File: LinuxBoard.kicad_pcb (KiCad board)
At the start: 2 copper layers, 5 parts, among them J1 Wuerth_7499010121A, U1 STM32MP151AAB3, U2 MT41K64M16TW-107_AAT_J_TR, U3 DP83848C, U4 STPMIC1APQR

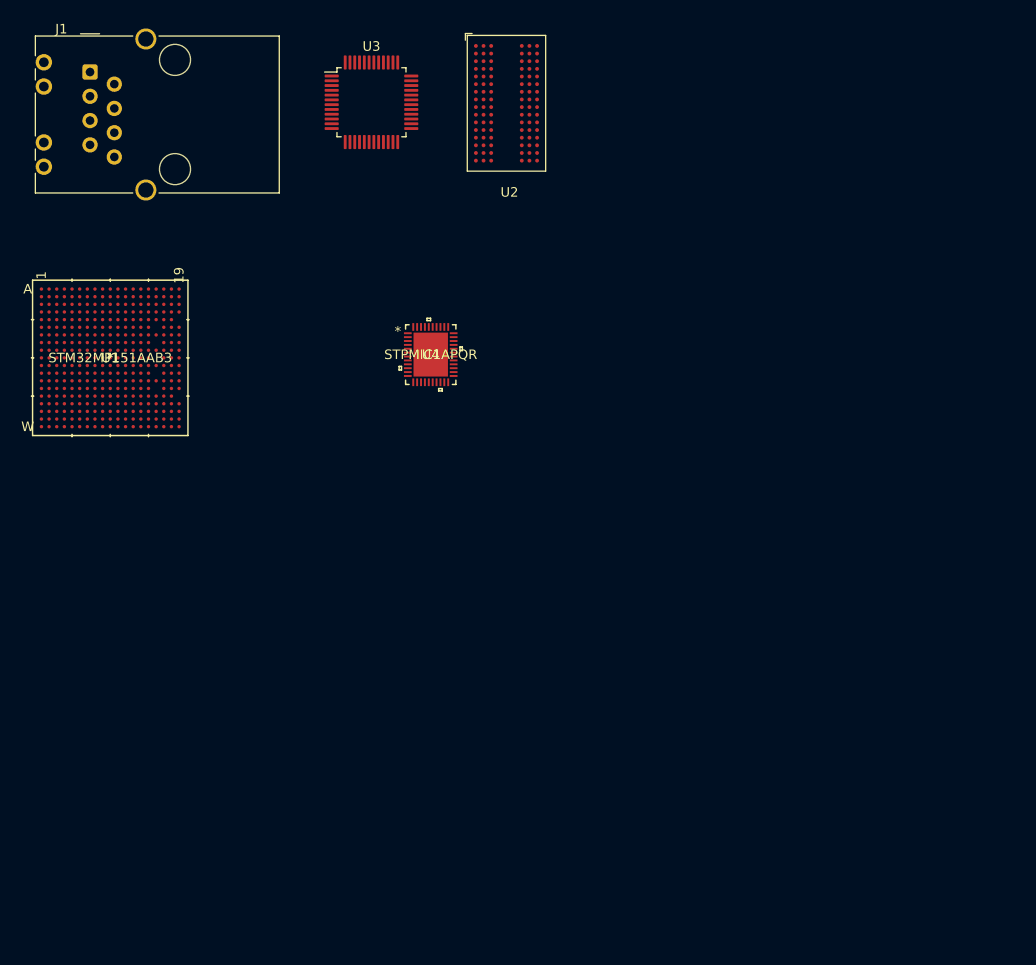
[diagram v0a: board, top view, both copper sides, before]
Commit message: Add bulk labels for RAM and ethernet
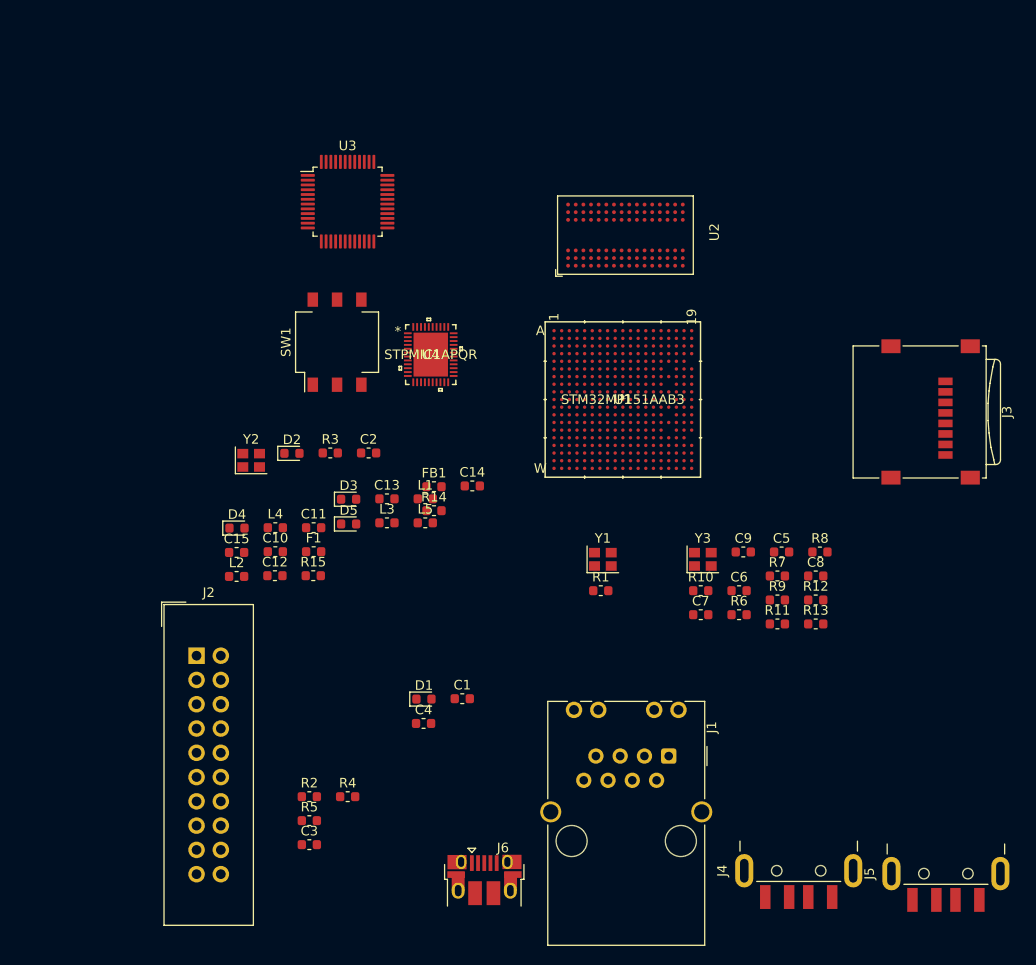
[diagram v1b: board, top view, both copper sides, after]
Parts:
- added C1: C, Capacitor_SMD:C_0603_1608Metric, F.Cu at (123.9, 100.9)
- added C10: C, Capacitor_SMD:C_0603_1608Metric, F.Cu at (104.3, 85.5)
- added C11: C, Capacitor_SMD:C_0603_1608Metric, F.Cu at (108.3, 83.0)
- added C12: C, Capacitor_SMD:C_0603_1608Metric, F.Cu at (104.3, 88.0)
- added C13: C, Capacitor_SMD:C_0603_1608Metric, F.Cu at (116.0, 80.0)
- added C14: C, Capacitor_SMD:C_0603_1608Metric, F.Cu at (125.0, 78.6)
- added C15: C, Capacitor_SMD:C_0603_1608Metric, F.Cu at (100.3, 85.6)
- added C2: C, Capacitor_SMD:C_0603_1608Metric, F.Cu at (114.1, 75.2)
- added C3: C, Capacitor_SMD:C_0603_1608Metric, F.Cu at (107.9, 116.2)
- added C4: C, Capacitor_SMD:C_0603_1608Metric, F.Cu at (119.8, 103.5)
- added C5: C, Capacitor_SMD:C_0603_1608Metric, F.Cu at (157.3, 85.5)
- added C6: C, Capacitor_SMD:C_0603_1608Metric, F.Cu at (152.9, 89.6)
- added C7: C, Capacitor_SMD:C_0603_1608Metric, F.Cu at (148.8, 92.1)
- added C8: C, Capacitor_SMD:C_0603_1608Metric, F.Cu at (160.9, 88.1)
- added C9: C, Capacitor_SMD:C_0603_1608Metric, F.Cu at (153.3, 85.5)
- added D1: LED, LED_SMD:LED_0603_1608Metric, F.Cu at (119.9, 100.9)
- added D2: LED, LED_SMD:LED_0603_1608Metric, F.Cu at (106.1, 75.2)
- added D3: D_Schottky, Diode_SMD:D_0603_1608Metric, F.Cu at (112.0, 80.0)
- added D4: LED, LED_SMD:LED_0603_1608Metric, F.Cu at (100.3, 83.0)
- added D5: LED, LED_SMD:LED_0603_1608Metric, F.Cu at (112.0, 82.6)
- added F1: Fuse, Fuse:Fuse_0603_1608Metric, F.Cu at (108.3, 85.5)
- added FB1: Ferrite_Bead, Inductor_SMD:L_0603_1608Metric, F.Cu at (120.9, 78.7)
- added J2: Conn_02x10_Counter_Clockwise, Connector_IDC:IDC-Header_2x10_P2.54mm_Vertical, F.Cu at (96.1, 96.4)
- added J3: Micro_SD_Card, Connector_Card:microSD_HC_Wuerth_693072010801, F.Cu at (172.9, 70.9)
- added J4: USB_A, Connector_USB:USB_A_CNCTech_1001-011-01101_Horizontal, F.Cu at (159.1, 112.0)
- added J5: USB_A, Connector_USB:USB_A_CNCTech_1001-011-01101_Horizontal, F.Cu at (174.5, 112.3)
- added J6: USB_B_Micro, Connector_USB:USB_Micro-B_Amphenol_10103594-0001LF_Horizontal, F.Cu at (126.2, 119.9)
- added L1: L, Inductor_SMD:L_0603_1608Metric, F.Cu at (120.0, 80.0)
- added L2: L, Inductor_SMD:L_0603_1608Metric, F.Cu at (100.3, 88.1)
- added L3: L, Inductor_SMD:L_0603_1608Metric, F.Cu at (116.0, 82.5)
- added L4: L, Inductor_SMD:L_0603_1608Metric, F.Cu at (104.3, 83.0)
- added L5: L, Inductor_SMD:L_0603_1608Metric, F.Cu at (120.0, 82.5)
- added R1: R, Resistor_SMD:R_0603_1608Metric, F.Cu at (138.4, 89.6)
- added R10: R, Resistor_SMD:R_0603_1608Metric, F.Cu at (148.8, 89.6)
- added R11: R, Resistor_SMD:R_0603_1608Metric, F.Cu at (156.9, 93.1)
- added R12: 2.2K, Resistor_SMD:R_0603_1608Metric, F.Cu at (160.9, 90.6)
- added R13: 2.2K, Resistor_SMD:R_0603_1608Metric, F.Cu at (160.9, 93.1)
- added R14: R, Resistor_SMD:R_0603_1608Metric, F.Cu at (120.9, 81.2)
- added R15: R, Resistor_SMD:R_0603_1608Metric, F.Cu at (108.3, 88.0)
- added R2: R, Resistor_SMD:R_0603_1608Metric, F.Cu at (107.9, 111.2)
- added R3: R, Resistor_SMD:R_0603_1608Metric, F.Cu at (110.1, 75.2)
- added R4: R, Resistor_SMD:R_0603_1608Metric, F.Cu at (111.9, 111.2)
- added R5: R, Resistor_SMD:R_0603_1608Metric, F.Cu at (107.9, 113.7)
- added R6: R, Resistor_SMD:R_0603_1608Metric, F.Cu at (152.9, 92.1)
- added R7: R, Resistor_SMD:R_0603_1608Metric, F.Cu at (156.9, 88.1)
- added R8: R, Resistor_SMD:R_0603_1608Metric, F.Cu at (161.3, 85.5)
- added R9: 4.87K, Resistor_SMD:R_0603_1608Metric, F.Cu at (156.9, 90.6)
- added SW1: SW_DIP_x03, Button_Switch_SMD:SW_DIP_SPSTx03_Slide_Omron_A6S-310x_W8.9mm_P2.54mm, F.Cu at (110.8, 63.6)
- added Y1: Crystal_GND24, Crystal:Crystal_SMD_2520-4Pin_2.5x2.0mm, F.Cu at (138.6, 86.3)
- added Y2: Crystal_GND24, Crystal:Crystal_SMD_2520-4Pin_2.5x2.0mm, F.Cu at (101.8, 76.0)
- added Y3: 25MHz, Crystal:Crystal_SMD_2520-4Pin_2.5x2.0mm, F.Cu at (149.1, 86.3)
- moved J1 93.7 mm to (145.5, 106.9), turned to 270 degrees
- moved U1 53.8 mm to (140.7, 69.6)
- moved U2 21.8 mm to (133.5, 52.4), turned to 90 degrees
- moved U3 10.7 mm to (111.9, 48.9)
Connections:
- net Net-(J1-Pad4) renamed /Ethernet/RD_P
- net Net-(J1-Pad6) renamed /Ethernet/RD_N
- net Net-(U1-PadA8) renamed /MPU/USART1_RX_TO_MPU
- net Net-(U1-PadB5) renamed /MPU/I2C_SDA
- net Net-(U1-PadC8) renamed /MPU/USART1_TX_FROM_MPU
- net Net-(U1-PadD7) renamed /MPU/USART2_TX_FROM_M4
- net Net-(U1-PadE3) renamed /MPU/USART2_RX_TO_M4
- net Net-(U1-PadF1) renamed /MPU/ETH1_PHY_INTN
- net Net-(U1-PadM4) renamed /RAM/A15
- net Net-(U1-PadP3) renamed /MPU/ETH1_COL
- net Net-(U1-PadP4) renamed /MPU/DAC1_OUT2
- net Net-(U1-PadR3) renamed /MPU/ETH1_CRS
- net Net-(U1-PadR4) renamed /MPU/DAC1_OUT1
- net Net-(U1-PadR7) renamed /RAM/A13
- net Net-(U1-PadT1) renamed /MPU/ETH1_TXD3
- net Net-(U1-PadT12) renamed /MPU/I2C_SCL
- net Net-(U1-PadT2) renamed /MPU/ETH1_TXD2
- net Net-(U1-PadT3) renamed /MPU/ETH1_TX_CLK
- net Net-(U1-PadT6) renamed /MPU/ETH1_RX_DV
- net Net-(U1-PadT9) renamed /MPU/ETH1_TXD1
- net Net-(U1-PadU2) renamed /MPU/ETH1_TXD0
- net Net-(U1-PadU4) renamed /MPU/ETH1_RX_CLK
- net Net-(U1-PadV1) renamed /MPU/ETH1_TX_EN
- net Net-(U1-PadV13) renamed /MPU/USB2_N
- net Net-(U1-PadV14) renamed /MPU/USB1_P
- net Net-(U1-PadV2) renamed /MPU/ETH1_MDC
- net Net-(U1-PadV3) renamed /MPU/ETH1_RXD3
- net Net-(U1-PadV4) renamed /MPU/ETH1_RXD1
- net Net-(U1-PadW13) renamed /MPU/USB2_P
- net Net-(U1-PadW14) renamed /MPU/USB1_N
- net Net-(U1-PadW2) renamed /MPU/ETH1_MDIO
- net Net-(U1-PadW3) renamed /MPU/ETH1_RXD2
- net Net-(U1-PadW4) renamed /MPU/ETH1_RXD0
- net Net-(U1-PadW5) renamed /MPU/ETH1_RX_ER
- net Net-(U2-PadA2) renamed /RAM/DQ13
- net Net-(U2-PadA3) renamed /RAM/DQ15
- net Net-(U2-PadA7) renamed /RAM/DQ12
- net Net-(U2-PadB8) renamed /RAM/DQ14
- net Net-(U2-PadC2) renamed /RAM/DQ11
- net Net-(U2-PadC3) renamed /RAM/DQ9
- net Net-(U2-PadC8) renamed /RAM/DQ10
- net Net-(U2-PadD7) renamed /RAM/DQ8
- net Net-(U2-PadE3) renamed /RAM/DQ0
- net Net-(U2-PadF2) renamed /RAM/DQ2
- net Net-(U2-PadF7) renamed /RAM/DQ1
- net Net-(U2-PadF8) renamed /RAM/DQ3
- net Net-(U2-PadG2) renamed /RAM/DQ6
- net Net-(U2-PadH3) renamed /RAM/DQ4
- net Net-(U2-PadH7) renamed /RAM/DQ7
- net Net-(U2-PadH8) renamed /RAM/DQ5
- net Net-(U3-Pad1) renamed /Ethernet/TX_CLK
- net Net-(U3-Pad2) renamed /Ethernet/TX_EN
- net Net-(U3-Pad29) renamed /Ethernet/ETH_RESET_N
- net Net-(U3-Pad3) renamed /Ethernet/TXD_0
- net Net-(U3-Pad30) renamed /Ethernet/MDIO
- net Net-(U3-Pad31) renamed /Ethernet/MDC
- net Net-(U3-Pad38) renamed /Ethernet/RX_CLK
- net Net-(U3-Pad39) renamed /Ethernet/RX_DV
- net Net-(U3-Pad4) renamed /Ethernet/TXD_1
- net Net-(U3-Pad41) renamed /Ethernet/RX_ER
- net Net-(U3-Pad43) renamed /Ethernet/RXD_0
- net Net-(U3-Pad44) renamed /Ethernet/RXD_1
- net Net-(U3-Pad45) renamed /Ethernet/RXD_2
- net Net-(U3-Pad46) renamed /Ethernet/RXD_3
- net Net-(U3-Pad5) renamed /Ethernet/TXD_2
- net Net-(U3-Pad6) renamed /Ethernet/TXD_3
- net Net-(U3-Pad7) renamed /Ethernet/ETH_PWR_DOWN
- net Net-(U4-Pad1) renamed /PMIC/PMIC_RESET_N
- net Net-(U4-Pad14) renamed /PMIC/VTT_DDR3
- net Net-(U4-Pad16) renamed /PMIC/VREF_DDR
- net Net-(U4-Pad17) renamed /PMIC/PMIC_PONKEY_N
- net Net-(U4-Pad18) renamed /PMIC/VOUT_LDO2
- net Net-(U4-Pad2) renamed /PMIC/PMIC_WAKEUP
- net Net-(U4-Pad20) renamed /PMIC/VOUT_LDO5
- net Net-(U4-Pad21) renamed /PMIC/VOUT_LDO6
- net Net-(U4-Pad23) renamed /PMIC/VOUT_LDO1
- net Net-(U4-Pad3) renamed /PMIC/I2C_SDA
- net Net-(U4-Pad38) renamed /PMIC/VBUS_HOST
- net Net-(U4-Pad39) renamed /PMIC/VDD_USB
- net Net-(U4-Pad4) renamed /PMIC/I2C_SCL
- net Net-(U4-Pad43) renamed /PMIC/PMIC_INT_N
- net Net-(U4-Pad44) renamed /PMIC/PMIC_PWRCTRL
- J1 pad 1: Net-(J1-Pad1) -> /Ethernet/TD_P
- J1 pad 10: Net-(J1-Pad10) -> /Ethernet/LED_GREEN
- J1 pad 12: Net-(J1-Pad12) -> /Ethernet/LED_YELLOW
- J1 pad 2: Net-(J1-Pad2) -> /Ethernet/RCT
- J1 pad 3: Net-(J1-Pad3) -> /Ethernet/TD_N
- J1 pad 5: Net-(J1-Pad5) -> /Ethernet/RCT
- J1 pad 8: Net-(J1-Pad8) -> GND
- J1 pad SH: Net-(J1-PadSH) -> GND
- U1 pad A10: Net-(U1-PadA10) -> /MPU/SD_D1
- U1 pad A11: Net-(U1-PadA11) -> /MPU/SD_D3
- U1 pad B10: Net-(U1-PadB10) -> /MPU/SD_CMD
- U1 pad B3: Net-(U1-PadB3) -> /MPU/SD_D2
- U1 pad C10: Net-(U1-PadC10) -> /MPU/SD_CK
- U1 pad C11: Net-(U1-PadC11) -> /MPU/SD_D0
- U1 pad E7: Net-(U1-PadE7) -> /RAM/BA0
- U1 pad E9: Net-(U1-PadE9) -> /RAM/BA1
- U1 pad F17: Net-(U1-PadF17) -> Net-(U1-PadE17)
- U1 pad F19: Net-(U1-PadF19) -> Net-(U1-PadE17)
- U1 pad F4: Net-(U1-PadF4) -> /RAM/BA2
- U1 pad G17: Net-(U1-PadG17) -> Net-(U1-PadE17)
- U1 pad G18: Net-(U1-PadG18) -> Net-(U1-PadE17)
- U1 pad G19: Net-(U1-PadG19) -> Net-(U1-PadE17)
- U1 pad H17: Net-(U1-PadH17) -> Net-(U1-PadE17)
- U1 pad H18: Net-(U1-PadH18) -> Net-(U1-PadE17)
- U1 pad J16: Net-(U1-PadJ16) -> Net-(U1-PadE17)
- U1 pad J19: Net-(U1-PadJ19) -> Net-(U1-PadE17)
- U1 pad K18: Net-(U1-PadK18) -> Net-(U1-PadE17)
- U1 pad K6: Net-(U1-PadK6) -> /RAM/A0
- U1 pad L16: Net-(U1-PadL16) -> Net-(U1-PadE17)
- U1 pad L17: Net-(U1-PadL17) -> Net-(U1-PadE17)
- U1 pad L5: Net-(U1-PadL5) -> /RAM/A1
- U1 pad L7: Net-(U1-PadL7) -> /RAM/A2
- U1 pad M17: Net-(U1-PadM17) -> Net-(U1-PadE17)
- U1 pad M18: Net-(U1-PadM18) -> Net-(U1-PadE17)
- U1 pad M19: Net-(U1-PadM19) -> Net-(U1-PadE17)
- U1 pad M6: Net-(U1-PadM6) -> /RAM/A3
- U1 pad M8: Net-(U1-PadM8) -> /RAM/A4
- U1 pad N16: Net-(U1-PadN16) -> Net-(U1-PadE17)
- U1 pad N17: Net-(U1-PadN17) -> Net-(U1-PadE17)
- U1 pad N18: Net-(U1-PadN18) -> Net-(U1-PadE17)
- U1 pad N5: Net-(U1-PadN5) -> /RAM/A5
- U1 pad N7: Net-(U1-PadN7) -> /RAM/A6
- U1 pad N9: Net-(U1-PadN9) -> /RAM/A7
- U1 pad P10: Net-(U1-PadP10) -> /RAM/A11
- U1 pad P17: Net-(U1-PadP17) -> Net-(U1-PadE17)
- U1 pad P6: Net-(U1-PadP6) -> /RAM/A8
- U1 pad P8: Net-(U1-PadP8) -> /RAM/A9
- U1 pad R11: Net-(U1-PadR11) -> /RAM/A12
- U1 pad R17: Net-(U1-PadR17) -> Net-(U1-PadE17)
- U1 pad R9: Net-(U1-PadR9) -> /RAM/A10
- U2 pad A1: Net-(U2-PadA1) -> /RAM/VDDQ
- U2 pad A8: Net-(U2-PadA8) -> /RAM/VDDQ
- U2 pad A9: Net-(U2-PadA9) -> GND
- U2 pad B1: Net-(U2-PadB1) -> GND
- U2 pad B2: Net-(U2-PadB2) -> /RAM/VDD
- U2 pad B3: Net-(U2-PadB3) -> GND
- U2 pad B9: Net-(U2-PadB9) -> GND
- U2 pad C1: Net-(U2-PadC1) -> /RAM/VDDQ
- U2 pad C9: Net-(U2-PadC9) -> /RAM/VDDQ
- U2 pad D1: Net-(U2-PadD1) -> GND
- U2 pad D2: Net-(U2-PadD2) -> /RAM/VDDQ
- U2 pad D8: Net-(U2-PadD8) -> GND
- U2 pad D9: Net-(U2-PadD9) -> /RAM/VDD
- U2 pad E1: Net-(U2-PadE1) -> GND
- U2 pad E2: Net-(U2-PadE2) -> GND
- U2 pad E8: Net-(U2-PadE8) -> GND
- U2 pad E9: Net-(U2-PadE9) -> /RAM/VDDQ
- U2 pad F1: Net-(U2-PadF1) -> /RAM/VDDQ
- U2 pad F9: Net-(U2-PadF9) -> GND
- U2 pad G1: Net-(U2-PadG1) -> GND
- U2 pad G7: Net-(U2-PadG7) -> /RAM/VDD
- U2 pad G8: Net-(U2-PadG8) -> GND
- U2 pad G9: Net-(U2-PadG9) -> GND
- U2 pad H2: Net-(U2-PadH2) -> /RAM/VDDQ
- U2 pad H9: Net-(U2-PadH9) -> /RAM/VDDQ
- U2 pad J2: Net-(U2-PadJ2) -> GND
- U2 pad J8: Net-(U2-PadJ8) -> GND
- U2 pad K2: Net-(U2-PadK2) -> /RAM/VDD
- U2 pad K8: Net-(U2-PadK8) -> /RAM/VDD
- U2 pad L7: Net-(U2-PadL7) -> /RAM/A10
- U2 pad M1: Net-(U2-PadM1) -> GND
- U2 pad M2: Net-(U2-PadM2) -> /RAM/BA0
- U2 pad M3: Net-(U2-PadM3) -> /RAM/BA2
- U2 pad M9: Net-(U2-PadM9) -> GND
- U2 pad N1: Net-(U2-PadN1) -> /RAM/VDD
- U2 pad N2: Net-(U2-PadN2) -> /RAM/A3
- U2 pad N3: Net-(U2-PadN3) -> /RAM/A0
- U2 pad N7: Net-(U2-PadN7) -> /RAM/A12
- U2 pad N8: Net-(U2-PadN8) -> /RAM/BA1
- U2 pad N9: Net-(U2-PadN9) -> /RAM/VDD
- U2 pad P1: Net-(U2-PadP1) -> GND
- U2 pad P2: Net-(U2-PadP2) -> /RAM/A5
- U2 pad P3: Net-(U2-PadP3) -> /RAM/A2
- U2 pad P7: Net-(U2-PadP7) -> /RAM/A1
- U2 pad P8: Net-(U2-PadP8) -> /RAM/A4
- U2 pad P9: Net-(U2-PadP9) -> GND
- U2 pad R1: Net-(U2-PadR1) -> /RAM/VDD
- U2 pad R2: Net-(U2-PadR2) -> /RAM/A7
- U2 pad R3: Net-(U2-PadR3) -> /RAM/A9
- U2 pad R7: Net-(U2-PadR7) -> /RAM/A11
- U2 pad R8: Net-(U2-PadR8) -> /RAM/A6
- U2 pad R9: Net-(U2-PadR9) -> /RAM/VDD
- U2 pad T1: Net-(U2-PadT1) -> GND
- U2 pad T8: Net-(U2-PadT8) -> /RAM/A8
- U2 pad T9: Net-(U2-PadT9) -> GND
- U3 pad 15: Net-(U3-Pad15) -> GND
- U3 pad 16: Net-(U3-Pad16) -> /Ethernet/TD_N
- U3 pad 17: Net-(U3-Pad17) -> /Ethernet/TD_P
- U3 pad 19: Net-(U3-Pad19) -> GND
- U3 pad 26: Net-(U3-Pad26) -> /Ethernet/LED_YELLOW
- U3 pad 28: Net-(U3-Pad28) -> /Ethernet/LED_GREEN
- U3 pad 35: Net-(U3-Pad35) -> GND
- U3 pad 36: Net-(U3-Pad36) -> GND
- U3 pad 47: Net-(U3-Pad47) -> GND
- U3 pad 48: Net-(U3-Pad48) -> Net-(U3-Pad32)
- U4 pad 10: Net-(U4-Pad10) -> GND
- U4 pad 12: Net-(U4-Pad12) -> /PMIC/V_USB_IN
- U4 pad 13: Net-(U4-Pad13) -> /PMIC/VDD_DDR
- U4 pad 15: Net-(U4-Pad15) -> GND
- U4 pad 19: Net-(U4-Pad19) -> /PMIC/V_USB_IN
- U4 pad 22: Net-(U4-Pad22) -> /PMIC/V_USB_IN
- U4 pad 24: Net-(U4-Pad24) -> /PMIC/V_USB_IN
- U4 pad 26: Net-(U4-Pad26) -> GND
- U4 pad 27: Net-(U4-Pad27) -> /PMIC/VDD_AUX
- U4 pad 28: Net-(U4-Pad28) -> /PMIC/V_USB_IN
- U4 pad 30: Net-(U4-Pad30) -> GND
- U4 pad 31: Net-(U4-Pad31) -> /PMIC/VDD
- U4 pad 32: Net-(U4-Pad32) -> GND
- U4 pad 33: Net-(U4-Pad33) -> /PMIC/VLXBST
- U4 pad 36: Net-(U4-Pad36) -> /PMIC/V_USB_IN
- U4 pad 37: Net-(U4-Pad37) -> Net-(U4-Pad34)
- U4 pad 41: Net-(U4-Pad41) -> GND
- U4 pad 42: Net-(U4-Pad42) -> /PMIC/VDD
- U4 pad 45: Net-(U4-Pad45) -> GND
- U4 pad 5: Net-(U4-Pad5) -> /PMIC/VDD_CORE
- U4 pad 6: Net-(U4-Pad6) -> GND
- U4 pad 8: Net-(U4-Pad8) -> /PMIC/V_USB_IN
- U4 pad 9: Net-(U4-Pad9) -> /PMIC/VDD_DDR

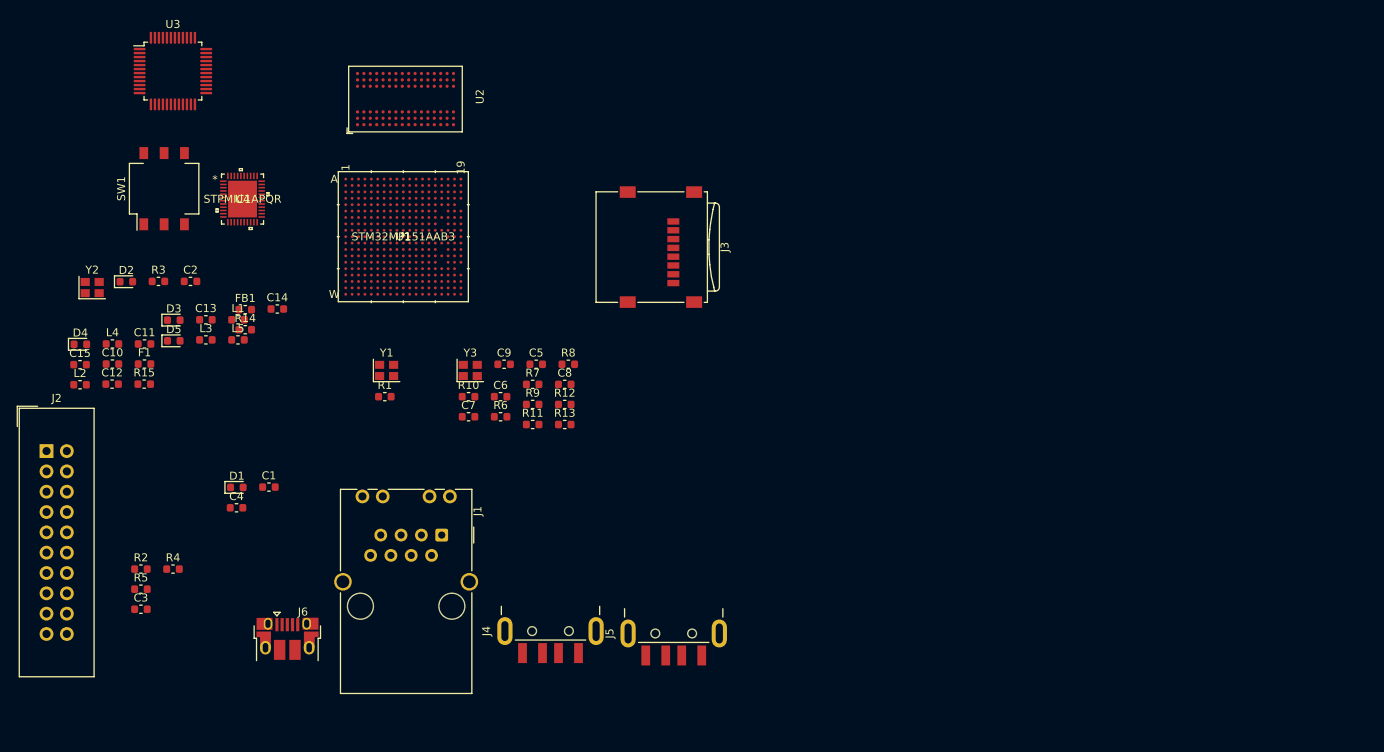
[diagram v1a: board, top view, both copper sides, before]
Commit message: Update footprints
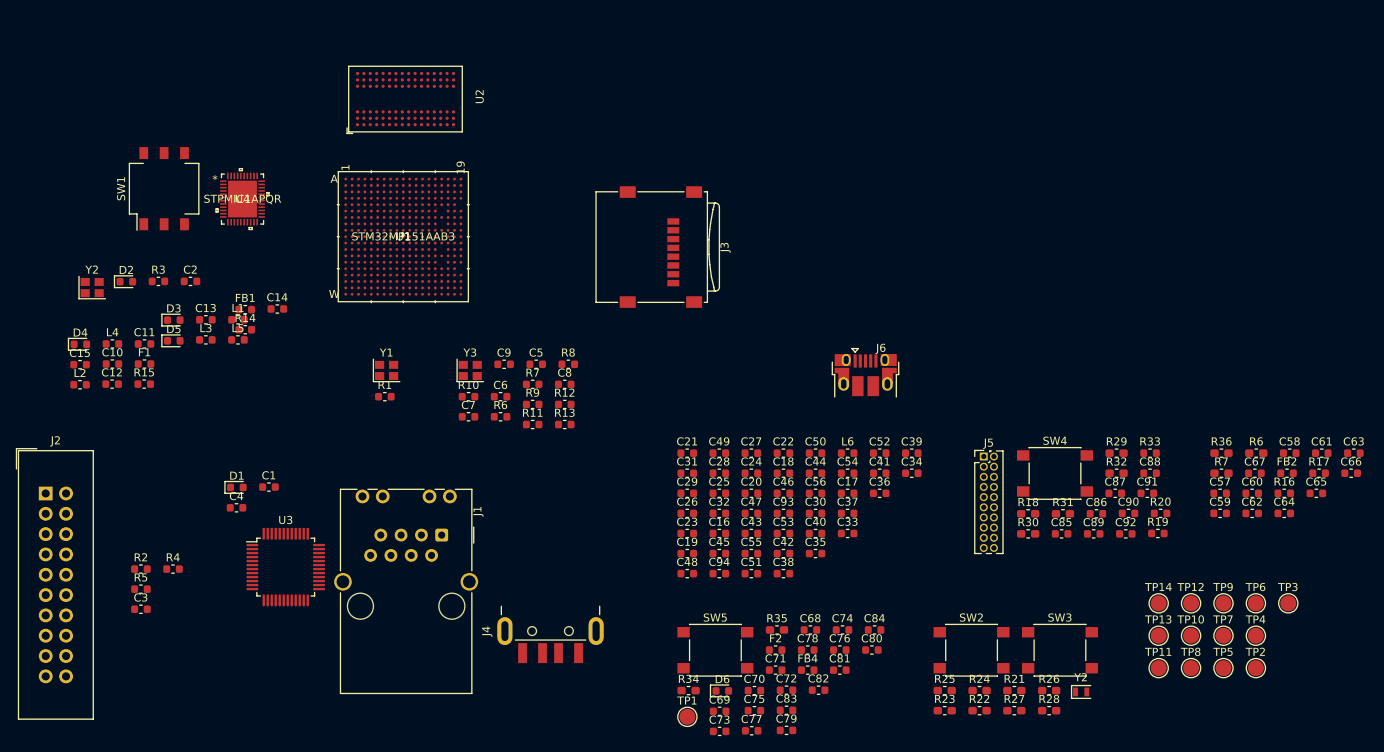
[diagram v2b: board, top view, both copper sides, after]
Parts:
- added C16: 1u, Capacitor_SMD:C_0603_1608Metric, F.Cu at (180.2, 106.7)
- added C17: 1n, Capacitor_SMD:C_0603_1608Metric, F.Cu at (196.2, 101.7)
- added C18: 1u, Capacitor_SMD:C_0603_1608Metric, F.Cu at (188.2, 99.2)
- added C19: 1u, Capacitor_SMD:C_0603_1608Metric, F.Cu at (176.2, 109.2)
- added C20: 1u, Capacitor_SMD:C_0603_1608Metric, F.Cu at (184.2, 101.7)
- added C21: 1n, Capacitor_SMD:C_0603_1608Metric, F.Cu at (176.2, 96.7)
- added C22: 1u, Capacitor_SMD:C_0603_1608Metric, F.Cu at (188.2, 96.7)
- added C23: 1u, Capacitor_SMD:C_0603_1608Metric, F.Cu at (176.2, 106.7)
- added C24: 1u, Capacitor_SMD:C_0603_1608Metric, F.Cu at (184.2, 99.2)
- added C25: 1u, Capacitor_SMD:C_0603_1608Metric, F.Cu at (180.2, 101.7)
- added C26: 1u, Capacitor_SMD:C_0603_1608Metric, F.Cu at (176.2, 104.2)
- added C27: 1u, Capacitor_SMD:C_0603_1608Metric, F.Cu at (184.2, 96.7)
- added C28: 1u, Capacitor_SMD:C_0603_1608Metric, F.Cu at (180.2, 99.2)
- added C29: 1u, Capacitor_SMD:C_0603_1608Metric, F.Cu at (176.2, 101.7)
- added C30: 1u, Capacitor_SMD:C_0603_1608Metric, F.Cu at (192.2, 104.2)
- added C31: 1u, Capacitor_SMD:C_0603_1608Metric, F.Cu at (176.2, 99.2)
- added C32: 2.2u, Capacitor_SMD:C_0603_1608Metric, F.Cu at (180.2, 104.2)
- added C33: 2.2u, Capacitor_SMD:C_0603_1608Metric, F.Cu at (196.2, 106.7)
- added C34: 1u, Capacitor_SMD:C_0603_1608Metric, F.Cu at (204.3, 99.2)
- added C35: 1u, Capacitor_SMD:C_0603_1608Metric, F.Cu at (192.2, 109.2)
- added C36: 1u, Capacitor_SMD:C_0603_1608Metric, F.Cu at (200.2, 101.7)
- added C37: 1u, Capacitor_SMD:C_0603_1608Metric, F.Cu at (196.2, 104.2)
- added C38: 1u, Capacitor_SMD:C_0603_1608Metric, F.Cu at (188.2, 111.7)
- added C39: 1u, Capacitor_SMD:C_0603_1608Metric, F.Cu at (204.3, 96.7)
- added C40: 1u, Capacitor_SMD:C_0603_1608Metric, F.Cu at (192.2, 106.7)
- added C41: 1u, Capacitor_SMD:C_0603_1608Metric, F.Cu at (200.2, 99.2)
- added C42: 1u, Capacitor_SMD:C_0603_1608Metric, F.Cu at (188.2, 109.2)
- added C43: 100n, Capacitor_SMD:C_0603_1608Metric, F.Cu at (184.2, 106.7)
- added C44: 100n, Capacitor_SMD:C_0603_1608Metric, F.Cu at (192.2, 99.2)
- added C45: 100n, Capacitor_SMD:C_0603_1608Metric, F.Cu at (180.2, 109.2)
- added C46: 1u, Capacitor_SMD:C_0603_1608Metric, F.Cu at (188.2, 101.7)
- added C47: 1u, Capacitor_SMD:C_0603_1608Metric, F.Cu at (184.2, 104.2)
- added C48: 1u, Capacitor_SMD:C_0603_1608Metric, F.Cu at (176.2, 111.7)
- added C49: 1u, Capacitor_SMD:C_0603_1608Metric, F.Cu at (180.2, 96.7)
- added C50: 1u, Capacitor_SMD:C_0603_1608Metric, F.Cu at (192.2, 96.7)
- added C51: 1u, Capacitor_SMD:C_0603_1608Metric, F.Cu at (184.2, 111.7)
- added C52: 1u, Capacitor_SMD:C_0603_1608Metric, F.Cu at (200.2, 96.7)
- added C53: 1u, Capacitor_SMD:C_0603_1608Metric, F.Cu at (188.2, 106.7)
- added C54: 1u, Capacitor_SMD:C_0603_1608Metric, F.Cu at (196.2, 99.2)
- added C55: 1u, Capacitor_SMD:C_0603_1608Metric, F.Cu at (184.2, 109.2)
- added C56: 1u, Capacitor_SMD:C_0603_1608Metric, F.Cu at (192.2, 101.7)
- added C57: 10u, Capacitor_SMD:C_0603_1608Metric, F.Cu at (242.8, 101.7)
- added C58: 100n, Capacitor_SMD:C_0603_1608Metric, F.Cu at (251.5, 96.7)
- added C59: 100n, Capacitor_SMD:C_0603_1608Metric, F.Cu at (242.8, 104.2)
- added C60: 100n, Capacitor_SMD:C_0603_1608Metric, F.Cu at (246.8, 101.7)
- added C61: 10u, Capacitor_SMD:C_0603_1608Metric, F.Cu at (255.5, 96.7)
- added C62: 10u, Capacitor_SMD:C_0603_1608Metric, F.Cu at (246.8, 104.2)
- added C63: 100n, Capacitor_SMD:C_0603_1608Metric, F.Cu at (259.5, 96.7)
- added C64: 100n, Capacitor_SMD:C_0603_1608Metric, F.Cu at (250.8, 104.2)
- added C65: 100n, Capacitor_SMD:C_0603_1608Metric, F.Cu at (254.8, 101.7)
- added C66: 100n, Capacitor_SMD:C_0603_1608Metric, F.Cu at (259.2, 99.2)
- added C67: 10n, Capacitor_SMD:C_0603_1608Metric, F.Cu at (247.2, 99.2)
- added C68: 4.7u, Capacitor_SMD:C_0603_1608Metric, F.Cu at (191.6, 118.8)
- added C69: 4.7u, Capacitor_SMD:C_0603_1608Metric, F.Cu at (180.2, 128.9)
- added C70: 1u, Capacitor_SMD:C_0603_1608Metric, F.Cu at (184.6, 126.3)
- added C71: 4.7u, Capacitor_SMD:C_0603_1608Metric, F.Cu at (187.2, 123.8)
- added C72: 10u, Capacitor_SMD:C_0603_1608Metric, F.Cu at (188.6, 126.3)
- added C73: 4.7u, Capacitor_SMD:C_0603_1608Metric, F.Cu at (180.2, 131.4)
- added C74: 4.7u, Capacitor_SMD:C_0603_1608Metric, F.Cu at (195.6, 118.8)
- added C75: 220u, Capacitor_SMD:C_0603_1608Metric, F.Cu at (184.6, 128.8)
- added C76: 4.7u, Capacitor_SMD:C_0603_1608Metric, F.Cu at (195.3, 121.3)
- added C77: 10u, Capacitor_SMD:C_0603_1608Metric, F.Cu at (184.2, 131.4)
- added C78: 10u, Capacitor_SMD:C_0603_1608Metric, F.Cu at (191.2, 121.3)
- added C79: 10u, Capacitor_SMD:C_0603_1608Metric, F.Cu at (188.6, 131.3)
- added C80: 10u, Capacitor_SMD:C_0603_1608Metric, F.Cu at (199.3, 121.3)
- added C81: 10u, Capacitor_SMD:C_0603_1608Metric, F.Cu at (195.3, 123.8)
- added C82: 1u, Capacitor_SMD:C_0603_1608Metric, F.Cu at (192.6, 126.3)
- added C83: 1u, Capacitor_SMD:C_0603_1608Metric, F.Cu at (188.6, 128.8)
- added C84: 4.7u, Capacitor_SMD:C_0603_1608Metric, F.Cu at (199.6, 118.8)
- added C85: 100n, Capacitor_SMD:C_0603_1608Metric, F.Cu at (223.0, 106.8)
- added C86: 100n, Capacitor_SMD:C_0603_1608Metric, F.Cu at (227.3, 104.2)
- added C87: 100n, Capacitor_SMD:C_0603_1608Metric, F.Cu at (229.7, 101.7)
- added C88: 100n, Capacitor_SMD:C_0603_1608Metric, F.Cu at (234.0, 99.2)
- added C89: 100n, Capacitor_SMD:C_0603_1608Metric, F.Cu at (227.0, 106.8)
- added C90: 100n, Capacitor_SMD:C_0603_1608Metric, F.Cu at (231.3, 104.2)
- added C91: 100n, Capacitor_SMD:C_0603_1608Metric, F.Cu at (233.7, 101.7)
- added C92: C, Capacitor_SMD:C_0603_1608Metric, F.Cu at (231.0, 106.8)
- added C93: 100n, Capacitor_SMD:C_0603_1608Metric, F.Cu at (188.2, 104.2)
- added C94: 10n, Capacitor_SMD:C_0603_1608Metric, F.Cu at (180.2, 111.7)
- added D6: D_Schottky, Diode_SMD:D_0603_1608Metric, F.Cu at (180.6, 126.4)
- added F2: Fuse, Fuse:Fuse_0603_1608Metric, F.Cu at (187.2, 121.3)
- added FB2: Ferrite_Bead, Inductor_SMD:L_0603_1608Metric, F.Cu at (251.2, 99.2)
- added FB4: Ferrite_Bead, Inductor_SMD:L_0603_1608Metric, F.Cu at (191.2, 123.8)
- added L6: 4.7u, Inductor_SMD:L_0603_1608Metric, F.Cu at (196.2, 96.7)
- added R16: 220, Resistor_SMD:R_0603_1608Metric, F.Cu at (250.8, 101.7)
- added R17: 470, Resistor_SMD:R_0603_1608Metric, F.Cu at (255.2, 99.2)
- added R18: 10k, Resistor_SMD:R_0603_1608Metric_Pad1.05x0.95mm_HandSolder, F.Cu at (218.8, 104.2)
- added R19: 240, Resistor_SMD:R_0603_1608Metric, F.Cu at (235.0, 106.7)
- added R20: 240, Resistor_SMD:R_0603_1608Metric, F.Cu at (235.4, 104.2)
- added R21: 0, Resistor_SMD:R_0603_1608Metric_Pad1.05x0.95mm_HandSolder, F.Cu at (217.1, 126.3)
- added R22: 0, Resistor_SMD:R_0603_1608Metric_Pad1.05x0.95mm_HandSolder, F.Cu at (212.7, 128.8)
- added R23: 10k, Resistor_SMD:R_0603_1608Metric_Pad1.05x0.95mm_HandSolder, F.Cu at (208.4, 128.8)
- added R24: 4.7k, Resistor_SMD:R_0603_1608Metric_Pad1.05x0.95mm_HandSolder, F.Cu at (212.7, 126.3)
- added R25: 4.7k, Resistor_SMD:R_0603_1608Metric_Pad1.05x0.95mm_HandSolder, F.Cu at (208.4, 126.3)
- added R26: 4.7k, Resistor_SMD:R_0603_1608Metric_Pad1.05x0.95mm_HandSolder, F.Cu at (221.4, 126.3)
- added R27: 10k, Resistor_SMD:R_0603_1608Metric_Pad1.05x0.95mm_HandSolder, F.Cu at (217.1, 128.8)
- added R28: 4.7k, Resistor_SMD:R_0603_1608Metric_Pad1.05x0.95mm_HandSolder, F.Cu at (221.4, 128.8)
- added R29: 10k, Resistor_SMD:R_0603_1608Metric_Pad1.05x0.95mm_HandSolder, F.Cu at (229.9, 96.7)
- added R30: 10K, Resistor_SMD:R_0603_1608Metric_Pad1.05x0.95mm_HandSolder, F.Cu at (218.8, 106.8)
- added R31: 10K, Resistor_SMD:R_0603_1608Metric_Pad1.05x0.95mm_HandSolder, F.Cu at (223.2, 104.2)
- added R32: 10k, Resistor_SMD:R_0603_1608Metric_Pad1.05x0.95mm_HandSolder, F.Cu at (229.9, 99.2)
- added R33: 3K, Resistor_SMD:R_0603_1608Metric, F.Cu at (234.0, 96.7)
- added R34: 0, Resistor_SMD:R_0603_1608Metric_Pad1.05x0.95mm_HandSolder, F.Cu at (176.4, 126.3)
- added R35: 0, Resistor_SMD:R_0603_1608Metric_Pad1.05x0.95mm_HandSolder, F.Cu at (187.4, 118.8)
- added R36: DNP, Resistor_SMD:R_0603_1608Metric_Pad1.05x0.95mm_HandSolder, F.Cu at (243.0, 96.7)
- added R6: 220, Resistor_SMD:R_0603_1608Metric_Pad1.05x0.95mm_HandSolder, F.Cu at (247.3, 96.7)
- added R7: 470, Resistor_SMD:R_0603_1608Metric_Pad1.05x0.95mm_HandSolder, F.Cu at (243.0, 99.2)
- added SW2: SW_Push, Button_Switch_SMD:SW_Push_1P1T_NO_6x6mm_H9.5mm, F.Cu at (211.7, 121.3)
- added SW3: SW_Push, Button_Switch_SMD:SW_Push_1P1T_NO_6x6mm_H9.5mm, F.Cu at (222.8, 121.3)
- added SW4: SW_Push, Button_Switch_SMD:SW_Push_1P1T_NO_6x6mm_H9.5mm, F.Cu at (222.2, 99.2)
- added SW5: SW_Push, Button_Switch_SMD:SW_Push_1P1T_NO_6x6mm_H9.5mm, F.Cu at (179.7, 121.3)
- added TP1: TestPoint, TestPoint:TestPoint_Pad_D2.0mm, F.Cu at (176.2, 129.6)
- added TP10: TestPoint, TestPoint:TestPoint_Pad_D2.0mm, F.Cu at (239.2, 119.5)
- added TP11: TestPoint, TestPoint:TestPoint_Pad_D2.0mm, F.Cu at (235.1, 123.5)
- added TP12: TestPoint, TestPoint:TestPoint_Pad_D2.0mm, F.Cu at (239.2, 115.4)
- added TP13: TestPoint, TestPoint:TestPoint_Pad_D2.0mm, F.Cu at (235.1, 119.5)
- added TP14: TestPoint, TestPoint:TestPoint_Pad_D2.0mm, F.Cu at (235.1, 115.4)
- added TP2: TestPoint, TestPoint:TestPoint_Pad_D2.0mm, F.Cu at (247.3, 123.5)
- added TP3: TestPoint, TestPoint:TestPoint_Pad_D2.0mm, F.Cu at (251.3, 115.4)
- added TP4: TestPoint, TestPoint:TestPoint_Pad_D2.0mm, F.Cu at (247.3, 119.5)
- added TP5: TestPoint, TestPoint:TestPoint_Pad_D2.0mm, F.Cu at (243.2, 123.5)
- added TP6: TestPoint, TestPoint:TestPoint_Pad_D2.0mm, F.Cu at (247.3, 115.4)
- added TP7: TestPoint, TestPoint:TestPoint_Pad_D2.0mm, F.Cu at (243.2, 119.5)
- added TP8: TestPoint, TestPoint:TestPoint_Pad_D2.0mm, F.Cu at (239.2, 123.5)
- added TP9: TestPoint, TestPoint:TestPoint_Pad_D2.0mm, F.Cu at (243.2, 115.4)
- added Y2: 32.768KHz, Crystal:Crystal_SMD_TXC_9HT11-2Pin_2.0x1.2mm, F.Cu at (225.4, 126.5)
- C1, C2: value C -> 12p
- C10, C11, C12, C13: value C -> 2.2u
- C14: value C -> 4.7u
- C15: value C -> 10u
- C3, C4: value C -> 20p
- C5, C7, C9: value C -> 100n
- C6, C8: value C -> 33p
- J5: value USB_A -> Conn_ARM_JTAG_SWD_20; footprint Connector_USB:USB_A_CNCTech_1001-011-01101_Horizontal -> Connector_PinHeader_1.27mm:PinHeader_2x10_P1.27mm_Vertical
- L1, L2, L3, L4, L5: value L -> 1u
- R1, R14, R15, R2: value R -> 470
- R10, R11: value R -> 49.9
- R3, R4, R5: value R -> 10k
- R8: value R -> 0
- Y1: value Crystal_GND24 -> 24MHz
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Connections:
- net Net-(C6-Pad1) renamed /Ethernet/X1
- net Net-(R12-Pad2) renamed /Ethernet/RESERVED_1
- net Net-(R13-Pad2) renamed /Ethernet/RESERVED_2
- net Net-(R3-Pad1) renamed /MPU/BOOT2
- net Net-(R4-Pad1) renamed /MPU/BOOT1
- net Net-(R5-Pad2) renamed /MPU/BOOT0
- net Net-(R8-Pad1) renamed /Ethernet/X2
- net Net-(R9-Pad2) renamed /Ethernet/R_BIAS
- net Net-(U1-PadA7) renamed /MPU/SPI1_SCK
- net Net-(U1-PadB9) renamed /MPU/SPI1_MISO
- net Net-(U1-PadT8) renamed /MPU/SPI1_MOSI
- net Net-(U4-Pad34) renamed /PMIC/BSTOUT
- C1 pad 1: Net-(C1-Pad1) -> /MPU/OSC_IN
- C10 pad 1: /PMIC/VDD_CORE -> /MPU_Power/PMIC_VDD_CORE
- C11 pad 1: /PMIC/VDD_DDR -> /MPU_Power/VDDQ_DDR
- C12 pad 2: /PMIC/VDD -> /VDD
- C15 pad 1: /PMIC/V_USB_IN -> /PMIC/BUCK1IN
- C3 pad 1: Net-(C3-Pad1) -> /MPU/OSC32_IN
- C5 pad 1: /Ethernet/RCT -> /VDD
- C7 pad 1: /Ethernet/RCT -> /VDD
- C9 pad 1: /Ethernet/RCT -> /VDD
- D3 pad 1: Net-(D3-Pad1) -> /PMIC/BUCK1IN
- D4 pad 2: /PMIC/V_USB_IN -> /PMIC/BUCK1IN
- D5 pad 2: /PMIC/VDD -> /VDD
- F1 pad 1: /PMIC/V_USB_IN -> Net-(D3-Pad2)
- FB1 pad 2: Net-(D3-Pad1) -> Net-(FB1-Pad2)
- J1 pad 11: Net-(J1-Pad11) -> GND
- J1 pad 2: /Ethernet/RCT -> /VDD
- J1 pad 5: /Ethernet/RCT -> /VDD
- J1 pad 9: Net-(J1-Pad9) -> GND
- J2 pad 1: Net-(J2-Pad1) -> /VDD
- J2 pad 10: Net-(J2-Pad10) -> GND
- J2 pad 11: Net-(J2-Pad11) -> GND
- J2 pad 12: Net-(J2-Pad12) -> /MPU/USART2_RX_TO_M4
- J2 pad 13: Net-(J2-Pad13) -> /MPU/USART2_TX_FROM_M4
- J2 pad 14: Net-(J2-Pad14) -> /MPU/DAC1_OUT2
- J2 pad 15: Net-(J2-Pad15) -> /MPU/GPIO8
- J2 pad 16: Net-(J2-Pad16) -> /MPU/GPIO7
- J2 pad 17: Net-(J2-Pad17) -> /MPU/ADC_IN1
- J2 pad 18: Net-(J2-Pad18) -> /MPU/GPIO6
- J2 pad 19: Net-(J2-Pad19) -> /MPU/GPIO5
- J2 pad 2: Net-(J2-Pad2) -> /MPU/GPIO1
- J2 pad 20: Net-(J2-Pad20) -> /MPU/DAC1_OUT1
- J2 pad 3: Net-(J2-Pad3) -> /MPU/GPIO2
- J2 pad 4: Net-(J2-Pad4) -> /MPU/GPIO3
- J2 pad 5: Net-(J2-Pad5) -> /MPU/GPIO4
- J2 pad 6: Net-(J2-Pad6) -> /MPU/I2C2_SCL
- J2 pad 7: Net-(J2-Pad7) -> /MPU/I2C2_SDA
- J2 pad 8: Net-(J2-Pad8) -> /MPU/USART1_TX_FROM_MPU
- J2 pad 9: Net-(J2-Pad9) -> /MPU/USART1_RX_TO_MPU
- J3 pad 4: Net-(J3-Pad4) -> /VDD
- J4 pad 1: Net-(J4-Pad1) -> /MPU/VBUS_HOST
- J4 pad 2: Net-(J4-Pad2) -> /MPU/USB1_N
- J4 pad 3: Net-(J4-Pad3) -> /MPU/USB1_P
- J5 pad 1: Net-(J5-Pad1) -> /VDD
- J5 pad 2: Net-(J5-Pad2) -> /VDD
- J5 pad 3: Net-(J5-Pad3) -> /RAM/NJTRST
- J5 pad 5: GND -> /RAM/JTDI
- J6 pad 1: Net-(D3-Pad2) -> Net-(FB1-Pad2)
- J6 pad 2: Net-(J6-Pad2) -> /MPU/USB2_N
- J6 pad 3: Net-(J6-Pad3) -> /MPU/USB2_P
- L1 pad 1: /PMIC/VDD_CORE -> /MPU_Power/PMIC_VDD_CORE
- L2 pad 1: /PMIC/VDD_DDR -> /MPU_Power/VDDQ_DDR
- L3 pad 2: /PMIC/VDD -> /VDD
- L5 pad 1: /PMIC/V_USB_IN -> Net-(L5-Pad1)
- L5 pad 2: /PMIC/VLXBST -> /PMIC/BUCK1IN
- R10 pad 2: /Ethernet/RCT -> /VDD
- R11 pad 1: /Ethernet/RCT -> /VDD
- R12 pad 1: /Ethernet/RCT -> /VDD
- R13 pad 1: /Ethernet/RCT -> /VDD
- SW1 pad 1: Net-(SW1-Pad1) -> /VDD
- SW1 pad 2: Net-(SW1-Pad2) -> /VDD
- SW1 pad 3: Net-(SW1-Pad3) -> /VDD
- U1 pad A1: Net-(U1-PadA1) -> GND
- U1 pad A17: Net-(U1-PadA17) -> /RAM/DQ0
- U1 pad A18: Net-(U1-PadA18) -> /RAM/DQ1
- U1 pad A19: Net-(U1-PadA19) -> GND
- U1 pad A2: Net-(U1-PadA2) -> /MPU/I2C2_SDA
- U1 pad B17: Net-(U1-PadB17) -> /RAM/DQ3
- U1 pad B18: Net-(U1-PadB18) -> /RAM/DQ7
- U1 pad B19: Net-(U1-PadB19) -> /RAM/LDQS_N
- U1 pad B2: Net-(U1-PadB2) -> GND
- U1 pad B4: Net-(U1-PadB4) -> /MPU/I2C2_SCL
- U1 pad B6: Net-(U1-PadB6) -> GND
- U1 pad C12: Net-(U1-PadC12) -> GND
- U1 pad C13: Net-(U1-PadC13) -> GND
- U1 pad C14: Net-(U1-PadC14) -> GND
- U1 pad C15: Net-(U1-PadC15) -> GND
- U1 pad C16: Net-(U1-PadC16) -> GND
- U1 pad C17: Net-(U1-PadC17) -> GND
- U1 pad C18: Net-(U1-PadC18) -> /RAM/LDM
- U1 pad C19: Net-(U1-PadC19) -> /RAM/LDQS_P
- U1 pad C3: Net-(U1-PadC3) -> GND
- U1 pad C5: Net-(U1-PadC5) -> /MPU/GPIO3
- U1 pad C6: Net-(U1-PadC6) -> /MPU/LED1
- U1 pad D1: Net-(U1-PadD1) -> GND
- U1 pad D12: Net-(U1-PadD12) -> /RAM/NJTRST
- U1 pad D13: Net-(U1-PadD13) -> /RAM/JTDI
- U1 pad D14: Net-(U1-PadD14) -> /RAM/SWO
- U1 pad D15: Net-(U1-PadD15) -> /RAM/SWDIO
- U1 pad D16: Net-(U1-PadD16) -> /RAM/SWDCLK
- U1 pad D17: Net-(U1-PadD17) -> /RAM/DQ5
- U1 pad D18: Net-(U1-PadD18) -> /RAM/DQ2
- U1 pad D19: Net-(U1-PadD19) -> /RAM/DQ6
- U1 pad D2: Net-(U1-PadD2) -> /MPU/PMIC_WAKEUP
- U1 pad D4: Net-(U1-PadD4) -> GND
- U1 pad D5: Net-(U1-PadD5) -> GND
- U1 pad D6: Net-(U1-PadD6) -> /MPU/LED2
- U1 pad D8: Net-(U1-PadD8) -> GND
- U1 pad E10: Net-(U1-PadE10) -> GND
- U1 pad E11: Net-(U1-PadE11) -> /MPU_Power/PMIC_VDD_CORE
- U1 pad E12: Net-(U1-PadE12) -> GND
- U1 pad E13: Net-(U1-PadE13) -> /MPU_Power/PMIC_VDD_CORE
- U1 pad E14: Net-(U1-PadE14) -> GND
- U1 pad E15: Net-(U1-PadE15) -> /MPU_Power/VDDQ_DDR
- U1 pad E16: Net-(U1-PadE16) -> GND
- U1 pad E17: Net-(U1-PadE17) -> /RAM/A7
- U1 pad E18: Net-(U1-PadE18) -> /RAM/DQ4
- U1 pad E2: Net-(U1-PadE2) -> GND
- U1 pad E4: Net-(U1-PadE4) -> GND
- U1 pad E5: Net-(U1-PadE5) -> GND
- U1 pad E6: Net-(U1-PadE6) -> GND
- U1 pad E7: /RAM/BA0 -> /MPU_Power/PMIC_VDD_CORE
- U1 pad E8: Net-(U1-PadE8) -> GND
- U1 pad E9: /RAM/BA1 -> /MPU_Power/PMIC_VDD_CORE
- U1 pad F10: Net-(U1-PadF10) -> /MPU_Power/PMIC_VDD_CORE
- U1 pad F11: Net-(U1-PadF11) -> GND
- U1 pad F12: Net-(U1-PadF12) -> /MPU_Power/PMIC_VDD_CORE
- U1 pad F13: Net-(U1-PadF13) -> GND
- U1 pad F14: Net-(U1-PadF14) -> /MPU_Power/VDDQ_DDR
- U1 pad F15: Net-(U1-PadF15) -> GND
- U1 pad F17: Net-(U1-PadE17) -> Net-(U1-PadF17)
- U1 pad F18: Net-(U1-PadF18) -> /RAM/ST_ZQ
- U1 pad F19: Net-(U1-PadE17) -> /RAM/A3
- U1 pad F2: Net-(U1-PadF2) -> /MPU/GPIO1
- U1 pad F3: Net-(U1-PadF3) -> /MPU/GPIO7
- U1 pad F4: /RAM/BA2 -> /MPU_Power/PMIC_VDD_CORE
- U1 pad F5: Net-(U1-PadF5) -> GND
- U1 pad F6: Net-(U1-PadF6) -> /MPU_Power/PMIC_VDD_CORE
- U1 pad F7: Net-(U1-PadF7) -> GND
- U1 pad F8: Net-(U1-PadF8) -> /MPU_Power/PMIC_VDD_CORE
- U1 pad F9: Net-(U1-PadF9) -> GND
- U1 pad G1: Net-(U1-PadG1) -> /MPU/GPIO8
- U1 pad G10: Net-(U1-PadG10) -> GND
- U1 pad G11: Net-(U1-PadG11) -> /MPU_Power/PMIC_VDD_CORE
- U1 pad G12: Net-(U1-PadG12) -> GND
- U1 pad G13: Net-(U1-PadG13) -> /VDD
- U1 pad G14: Net-(U1-PadG14) -> GND
- U1 pad G15: Net-(U1-PadG15) -> /MPU_Power/VDDQ_DDR
- U1 pad G16: Net-(U1-PadG16) -> /RAM/RESET_N
- U1 pad G17: Net-(U1-PadE17) -> /RAM/A9
- U1 pad G18: Net-(U1-PadE17) -> /RAM/A2
- U1 pad G19: Net-(U1-PadE17) -> /RAM/BA0
- U1 pad G2: Net-(U1-PadG2) -> GND
- U1 pad G3: Net-(U1-PadG3) -> /MPU/GPIO2
- U1 pad G4: Net-(U1-PadG4) -> GND
- U1 pad G5: Net-(U1-PadG5) -> /MPU_Power/PMIC_VDD_CORE
- U1 pad G6: Net-(U1-PadG6) -> GND
- U1 pad G7: Net-(U1-PadG7) -> /MPU_Power/PMIC_VDD_CORE
- U1 pad G8: Net-(U1-PadG8) -> GND
- U1 pad G9: Net-(U1-PadG9) -> /MPU_Power/PMIC_VDD_CORE
- U1 pad H1: Net-(U1-PadH1) -> /MPU/OSC32_IN
- U1 pad H10: Net-(U1-PadH10) -> /MPU_Power/PMIC_VDD_CORE
- U1 pad H11: Net-(U1-PadH11) -> GND
- U1 pad H12: Net-(U1-PadH12) -> /MPU_Power/PMIC_VDD_CORE
- U1 pad H13: Net-(U1-PadH13) -> GND
- U1 pad H14: Net-(U1-PadH14) -> /MPU_Power/VDDQ_DDR
- U1 pad H15: Net-(U1-PadH15) -> GND
- U1 pad H17: Net-(U1-PadE17) -> /RAM/A5
- U1 pad H18: Net-(U1-PadE17) -> /RAM/A0
- U1 pad H19: Net-(U1-PadH19) -> /RAM/ODT
- U1 pad H2: Net-(U1-PadH2) -> /MPU/OSC32_OUT
- U1 pad H3: Net-(U1-PadH3) -> /VDD
- U1 pad H4: Net-(U1-PadH4) -> /MPU_Power/PMIC_VDD_CORE
- U1 pad H5: Net-(U1-PadH5) -> GND
- U1 pad H6: Net-(U1-PadH6) -> /MPU_Power/PMIC_VDD_CORE
- U1 pad H7: Net-(U1-PadH7) -> GND
- U1 pad H8: Net-(U1-PadH8) -> /MPU_Power/PMIC_VDD_CORE
- U1 pad H9: Net-(U1-PadH9) -> GND
- U1 pad J1: Net-(U1-PadJ1) -> /RAM/NRST
- U1 pad J10: Net-(U1-PadJ10) -> GND
- U1 pad J11: Net-(U1-PadJ11) -> /MPU_Power/PMIC_VDD_CORE
- U1 pad J12: Net-(U1-PadJ12) -> GND
- U1 pad J13: Net-(U1-PadJ13) -> /MPU_Power/PMIC_VDD_CORE
- U1 pad J14: Net-(U1-PadJ14) -> GND
- U1 pad J15: Net-(U1-PadJ15) -> /MPU_Power/VDDQ_DDR
- U1 pad J16: Net-(U1-PadE17) -> /RAM/BA2
- U1 pad J17: Net-(U1-PadJ17) -> /RAM/WE_N
- U1 pad J18: Net-(U1-PadJ18) -> /RAM/CS_N
- U1 pad J19: Net-(U1-PadE17) -> Net-(U1-PadJ19)
- U1 pad J2: Net-(U1-PadJ2) -> /RAM/NRST
- U1 pad J3: Net-(U1-PadJ3) -> GND
- U1 pad J4: Net-(U1-PadJ4) -> GND
- U1 pad J5: Net-(U1-PadJ5) -> /VDD
- U1 pad J6: Net-(U1-PadJ6) -> GND
- U1 pad J7: Net-(U1-PadJ7) -> /MPU_Power/PMIC_VDD_CORE
- U1 pad J8: Net-(U1-PadJ8) -> GND
- U1 pad J9: Net-(U1-PadJ9) -> /MPU_Power/PMIC_VDD_CORE
- U1 pad K10: Net-(U1-PadK10) -> /MPU_Power/PMIC_VDD_CORE
- U1 pad K11: Net-(U1-PadK11) -> GND
- U1 pad K12: Net-(U1-PadK12) -> /MPU_Power/PMIC_VDD_CORE
- U1 pad K13: Net-(U1-PadK13) -> GND
- U1 pad K14: Net-(U1-PadK14) -> /MPU_Power/VDDQ_DDR
- U1 pad K15: Net-(U1-PadK15) -> GND
- U1 pad K17: Net-(U1-PadK17) -> /RAM/CAS_N
- U1 pad K18: Net-(U1-PadE17) -> Net-(U1-PadK18)
- U1 pad K19: Net-(U1-PadK19) -> /RAM/CK_N
- U1 pad K2: Net-(U1-PadK2) -> GND
- U1 pad K3: Net-(U1-PadK3) -> /MPU/PMIC_INT_N
- U1 pad K5: Net-(U1-PadK5) -> GND
- U1 pad K6: /RAM/A0 -> /VDD
- U1 pad K7: Net-(U1-PadK7) -> GND
- U1 pad K8: Net-(U1-PadK8) -> /MPU_Power/PMIC_VDD_CORE
- U1 pad K9: Net-(U1-PadK9) -> GND
- U1 pad L1: Net-(U1-PadL1) -> /PMIC/PMIC_PWRCTRL
- U1 pad L10: Net-(U1-PadL10) -> GND
- U1 pad L11: Net-(U1-PadL11) -> /MPU_Power/PMIC_VDD_CORE
- U1 pad L12: Net-(U1-PadL12) -> GND
- U1 pad L13: Net-(U1-PadL13) -> /MPU_Power/PMIC_VDD_CORE
- U1 pad L14: Net-(U1-PadL14) -> GND
- U1 pad L15: Net-(U1-PadL15) -> /MPU_Power/VDDQ_DDR
- U1 pad L16: Net-(U1-PadE17) -> Net-(U1-PadL16)
- U1 pad L17: Net-(U1-PadE17) -> /RAM/A12
- U1 pad L18: Net-(U1-PadL18) -> /RAM/RAS_N
- U1 pad L19: Net-(U1-PadL19) -> /RAM/CK_P
- U1 pad L3: Net-(U1-PadL3) -> /VDD
- U1 pad L4: Net-(U1-PadL4) -> GND
- U1 pad L5: /RAM/A1 -> /VDD
- U1 pad L6: Net-(U1-PadL6) -> GND
- U1 pad L7: /RAM/A2 -> /VDD
- U1 pad L8: Net-(U1-PadL8) -> GND
- U1 pad L9: Net-(U1-PadL9) -> /MPU_Power/PMIC_VDD_CORE
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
